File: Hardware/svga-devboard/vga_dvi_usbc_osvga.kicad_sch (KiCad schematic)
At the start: 9 parts

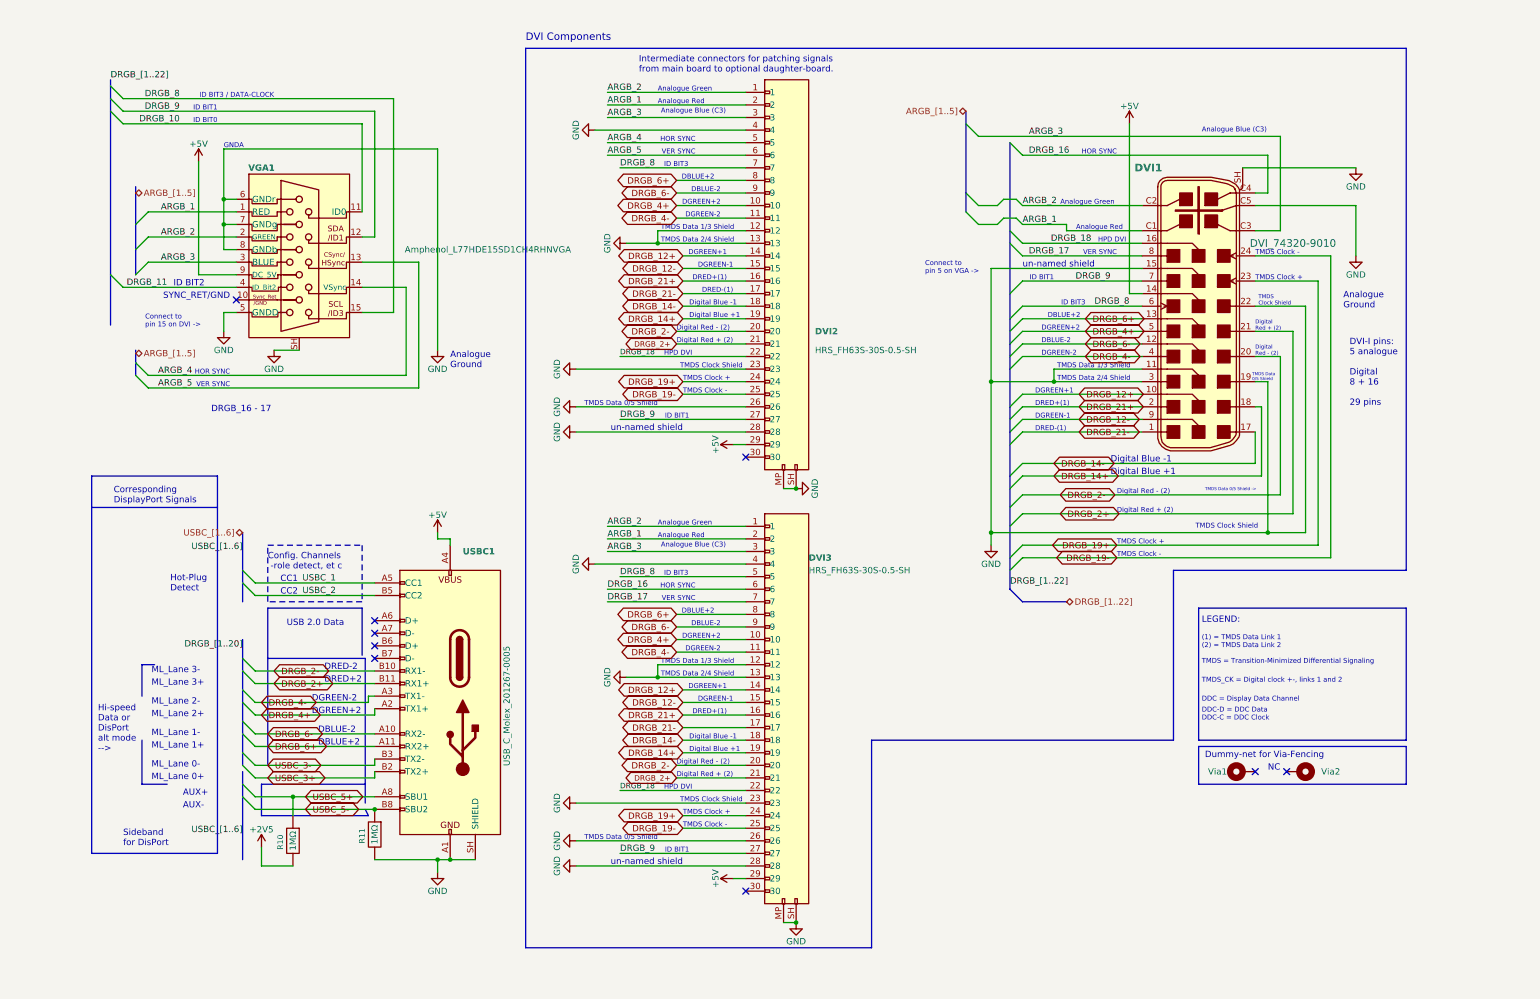
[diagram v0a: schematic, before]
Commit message: Disconnected the DVI-connectors from each other, so that they do go over the intended flat-cable to the daughter-board instead.
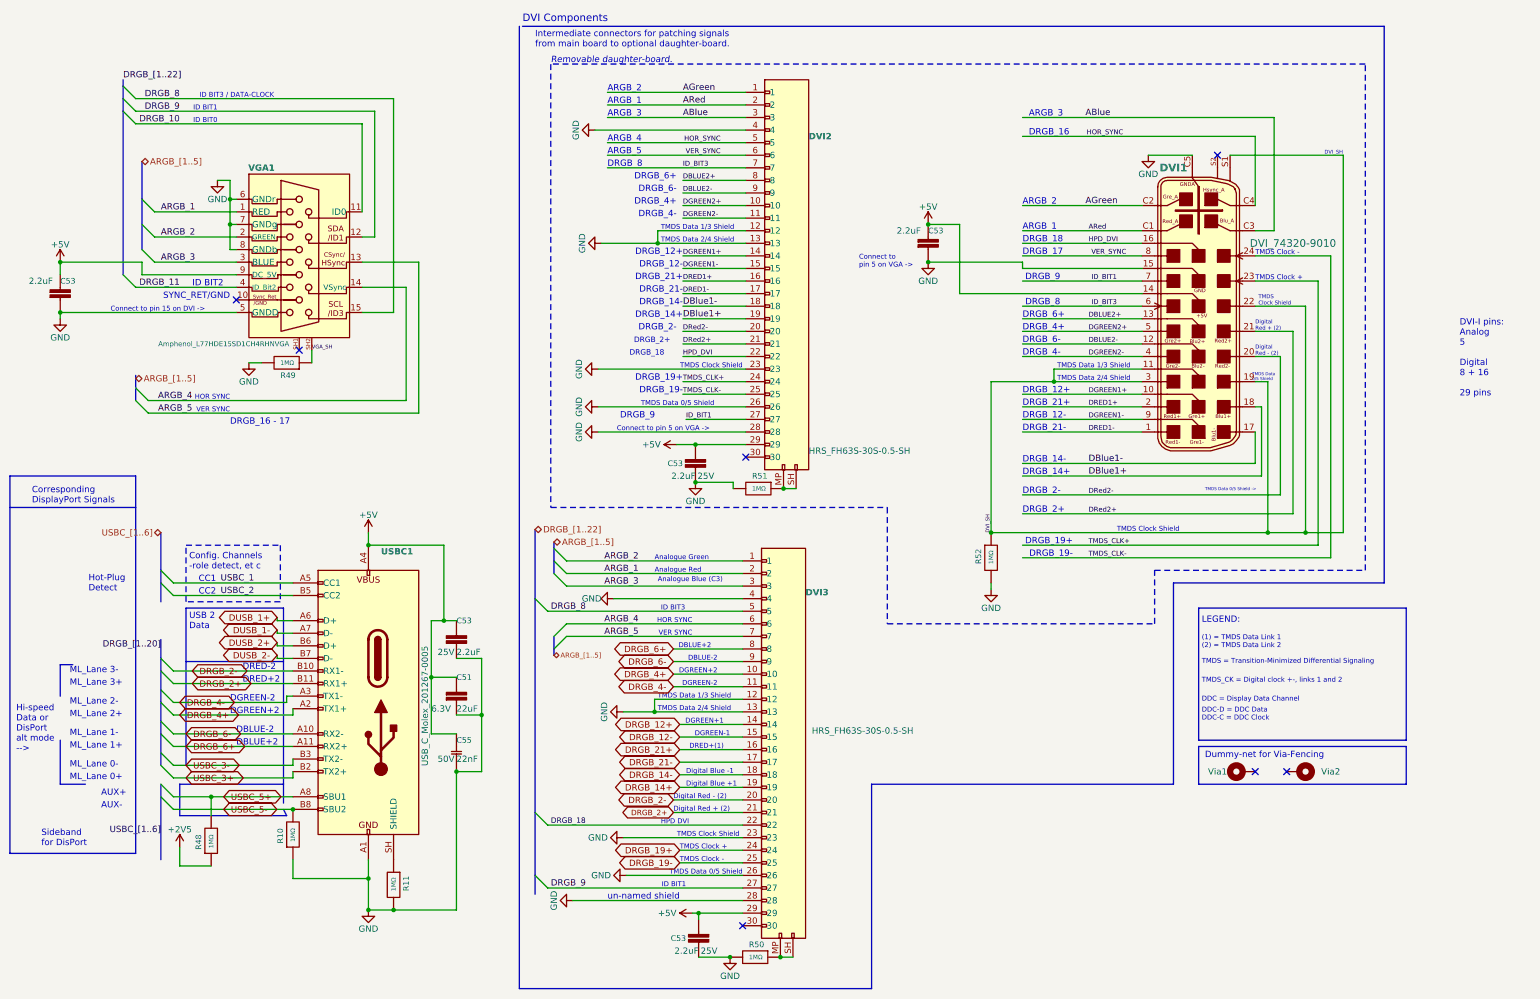
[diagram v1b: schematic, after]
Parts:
- removed R10, R11: R_CMP2010-FX-1004ELF, Resistor_SMD:R_2010_5025Metric_Pad1.40x2.65mm_HandSolder, symbol LRJ-parts:R_CMP2010-FX-1004ELF
- added C51: C_GRM188C80J226ME15D, Capacitor_SMD:C_0603_1608Metric, symbol LRJ-parts:C_GRM188C80J226ME15D
- added C53 (x5): C_CL21B225KAFNFNE, Capacitor_SMD:C_0805_2012Metric_Pad1.18x1.45mm_HandSolder, symbol LRJ-parts:C_CL21B225KAFNFNE
- added C55: C_CL21B223KBANFNC, Capacitor_SMD:C_0805_2012Metric_Pad1.18x1.45mm_HandSolder, symbol LRJ-parts:C_CL21B223KBANFNC
- added R10, R11, R48, R49, R50, R51, R52: R_ERJ-3GEYJ105V, Resistor_SMD:R_0603_1608Metric, symbol LRJ-parts:R_ERJ-3GEYJ105V
- DVI2, DVI3: footprint LRJ:Hirose_FH63S-30S-0.5SH_1x30-1MP_P0.50mm_Horizontal -> LRJ:Hirose_FH63S-30S-0.5SH_1x30-2MP_P0.50mm_Horizontal
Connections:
- net +2V5: now also R48.1
- net +5V: now also C51.1, C53.1, C53.1, C53.1, C53.2, C53.2, C55.1
- net ARGB_1: no longer DVI1.C1, DVI2.2
- net ARGB_2: no longer DVI1.C2, DVI2.1
- net ARGB_3: no longer DVI1.C3, DVI2.3
- net ARGB_4: now also DVI3.6; no longer DVI2.5
- net ARGB_5: now also DVI3.7; no longer DVI2.6
- net DRGB_12+: no longer DVI1.10, DVI2.14
- net DRGB_12-: no longer DVI1.9, DVI2.15
- net DRGB_14+: no longer DVI1.18, DVI2.19
- net DRGB_14-: no longer DVI1.17, DVI2.18
- net DRGB_18: no longer DVI1.16, DVI2.22
- net DRGB_19+: no longer DVI1.23, DVI2.24
- net DRGB_19-: no longer DVI1.24, DVI2.25
- net DRGB_2+: no longer DVI1.21, DVI2.21
- net DRGB_2-: no longer DVI1.20, DVI2.20
- net DRGB_21+: no longer DVI1.2, DVI2.16
- net DRGB_21-: no longer DVI1.1, DVI2.17
- net DRGB_4+: no longer DVI1.5, DVI2.10
- net DRGB_4-: no longer DVI1.4, DVI2.11
- net DRGB_6+: no longer DVI1.13, DVI2.8
- net DRGB_6-: no longer DVI1.12, DVI2.9
- net DRGB_8: no longer DVI1.6, DVI2.7
- net DRGB_9: no longer DVI1.7, DVI2.27
- net GND: now also C51.2, C53.1, C53.1, C53.2, C53.2, C53.2, C55.2, R10.1, R11.2, R49.2, R50.2, R51.2, R52.2; no longer DVI1.11, DVI1.19, DVI1.22, DVI1.3, DVI1.SH, DVI2.MP, DVI2.SH, DVI3.MP, DVI3.SH, USBC1.SH (SHIELD), VGA1.SH
- net USBC_5+: now also R48.2
- net USBC_5-: now also R10.2
- net DUSB_1+: now reaches USBC1.A6 (D+)
- net DUSB_1-: now reaches USBC1.A7 (D-)
- net DUSB_2+: now reaches USBC1.B6 (D+)
- net DUSB_2-: now reaches USBC1.B7 (D-)
- net DRGB_16 renamed HOR_SYNC
- net HOR_SYNC: now also DVI2.5; no longer DVI3.6
- net DRGB_17 renamed VER_SYNC
- net VER_SYNC: now also DVI2.6; no longer DVI3.7
- new net: R11.1, USBC1.SH (SHIELD)
- new net: DVI2.MP, DVI2.SH, R51.1
- new net: DVI3.MP, DVI3.SH, R50.1
- new net ABlue: DVI1.C3 (Analog_Blue), DVI2.3
- new net AGreen: DVI1.C2 (Analog_Green), DVI2.1
- new net ARed: DVI1.C1 (Analog_Red), DVI2.2
- new net DBLUE2+: DVI1.13 (Digital_Blue2+), DVI2.8
- new net DBLUE2-: DVI1.12 (Digital_Blue2-), DVI2.9
- new net DBlue1+: DVI1.18 (Digital_Blue1+), DVI2.19
- new net DBlue1-: DVI1.17 (Digital_Blue1-), DVI2.18
- new net DGREEN1+: DVI1.10 (Digital_Green1+), DVI2.14
- new net DGREEN1-: DVI1.9 (Digital_Green1-), DVI2.15
- new net DGREEN2+: DVI1.5 (Digital_Green2+), DVI2.10
- new net DGREEN2-: DVI1.4 (Digital_Green2-), DVI2.11
- new net DRED1+: DVI1.2 (Digital_Red1+), DVI2.16
- new net DRED1-: DVI1.1 (Digital_Red1-), DVI2.17
- new net DRed2+: DVI1.21 (Digital_Red2+), DVI2.21
- new net DRed2-: DVI1.20 (Digital_Red2-), DVI2.20
- new net DVI_SH: DVI1.11 (TMDS_Dat1-3_sh), DVI1.19 (TMDS_Dat0-5_sh), DVI1.22 (TMDS_CLK_sh), DVI1.3 (TMDS_Dat2-4_sh), DVI1.S1 (SHIELD), R52.1
- new net HPD_DVI: DVI1.16 (HPD), DVI2.22
- new net ID_BIT1: DVI1.7 (DDC_DAT), DVI2.27
- new net ID_BIT3: DVI1.6 (DDC_CLK), DVI2.7
- new net TMDS_CLK+: DVI1.23 (TMDS_CLK+), DVI2.24
- new net TMDS_CLK-: DVI1.24 (TMDS_CLK-), DVI2.25
- new net VGA_SH: R49.1, VGA1.SH2 (SH)
- no-connect marks 9 -> 7
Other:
- note added: "ARGB_1"
- note added: "ARGB_2"
- note added: "ARGB_3"
- note added: "ARGB_4"
- note added: "ARGB_5"
- note added: "DRGB_12+"
- note added: "DRGB_12-"
- note added: "DRGB_14+"
- note added: "DRGB_14-"
- note added: "DRGB_16"
- note added: "DRGB_17"
- note added: "DRGB_18"
- note added: "DRGB_19+"
- note added: "DRGB_19-"
- note added: "DRGB_2+"
- note added: "DRGB_2-"
- note added: "DRGB_21+"
- note added: "DRGB_21-"
- note added: "DRGB_4+"
- note added: "DRGB_4-"
- note added: "DRGB_6+"
- note added: "DRGB_6-"
- note added: "DRGB_8"
- note added: "DRGB_9"
- note added: "DVI-I pins: Analog 5 Digital 8 + 16 29 pins"
- note added: "DVI_SH"
- note added: "Removable daughter-board."
- note added: "USB 2 Data"
- note removed: "Analogue Ground"
- note removed: "DRED-(1)"
- note removed: "DVI-I pins: 5 analogue Digital 8 + 16 29 pins"
- note removed: "GNDA"
- note removed: "NC"
- note removed: "USB 2.0 Data"
- moved on the sheet: DVI3, USBC1
